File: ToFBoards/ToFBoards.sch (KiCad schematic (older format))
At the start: 1 part, among them U1 VL53L1X

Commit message: ToF boards
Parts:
- added C1: 100n, Capacitors_SMD:C_0402, symbol C_Small
- added C2: 4.7u, Capacitors_SMD:C_0402, symbol C_Small
- added J1: Bottom, footprint:ToFTop, symbol Conn_01x02
- added J2: Top, footprint:ToFBottom, symbol Conn_01x03
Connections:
- net VCC: now reaches U1.1 (AVDDS)
- net VCC: now also U1.11 (AVDD), C1.1, C2.1, J2.1 (Pin_1)
- net SCL: now reaches U1.10 (SCL)
- net SCL: now also J1.1 (Pin_1)
- net GND: now reaches U1.12 (GND4)
- net GND: now also U1.2 (AVSSS), U1.3 (GND1), U1.4 (GND2), U1.6 (GND3), C1.2, C2.2, J2.3 (Pin_3)
- net SIGNAL: now reaches U1.5 (XSHUT)
- net SIGNAL: now also J1.2 (Pin_2)
- net SDA: now reaches U1.9 (SDA)
- net SDA: now also J2.2 (Pin_2)
- no-connect marks 0 -> 2
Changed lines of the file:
@@
 LIBS:valves
 LIBS:parts
+LIBS:ToFBoards-cache
 EELAYER 25 0
 EELAYER END
@@
 	1    0    0    -1
 $EndComp
+Text GLabel 6185 3545 2    39   Input ~ 0
+SCL
+Text GLabel 6185 3755 2    39   Input ~ 0
+SDA
+$Comp
+L C_Small C2
+U 1 1 5B60667F
+P 4530 3220
+F 0 "C2" H 4540 3290 39  0000 L CNN
+F 1 "4.7u" H 4540 3140 39  0000 L CNN
+F 2 "Capacitors_SMD:C_0402" H 4530 3220 50  0001 C CNN
+F 3 "" H 4530 3220 50  0001 C CNN
+	1    4530 3220
+	1    0    0    -1
+$EndComp
+$Comp
+L C_Small C1
+U 1 1 5B606704
+P 4100 3220
+F 0 "C1" H 4110 3290 39  0000 L CNN
+F 1 "100n" H 4110 3140 39  0000 L CNN
+F 2 "Capacitors_SMD:C_0402" H 4100 3220 50  0001 C CNN
+F 3 "" H 4100 3220 50  0001 C CNN
+	1    4100 3220
+	1    0    0    -1
+$EndComp
+Text GLabel 3895 3100 0    39   Input ~ 0
+VCC
+Text GLabel 3895 3650 0    39   Input ~ 0
+GND
+Text GLabel 5145 3860 0    39   Input ~ 0
+SIGNAL
+NoConn ~ 6185 3855
+NoConn ~ 6185 3960
+Wire Wire Line
+	5145 3960 4835 3960
+Wire Wire Line
+	4835 3545 4835 4250
+Wire Wire Line
+	4835 3755 5145 3755
+Wire Wire Line
+	6185 3435 6420 3435
+Wire Wire Line
+	6420 3435 6420 4250
+Wire Wire Line
+	6420 4250 4835 4250
+Connection ~ 4835 3960
+Wire Wire Line
+	3895 3100 6565 3100
+Wire Wire Line
+	4100 3100 4100 3120
+Wire Wire Line
+	4530 3100 4530 3120
+Connection ~ 4100 3100
+Wire Wire Line
+	6565 3100 6565 3650
+Wire Wire Line
+	6565 3650 6185 3650
+Connection ~ 4530 3100
+Wire Wire Line
+	5145 3435 4940 3435
+Wire Wire Line
+	4940 3435 4940 3100
+Connection ~ 4940 3100
+Wire Wire Line
+	4100 3320 4100 3650
+Wire Wire Line
+	3895 3650 5145 3650
+Connection ~ 4100 3650
+Connection ~ 4835 3650
+Connection ~ 4835 3755
+Wire Wire Line
+	4530 3545 5145 3545
+Wire Wire Line
+	4530 3320 4530 3545
+Connection ~ 4835 3545
+$Comp
+L Conn_01x02 J1
+U 1 1 5B606E26
+P 8025 3300
+F 0 "J1" H 8025 3400 50  0000 C CNN
+F 1 "Bottom" H 8025 3100 50  0000 C CNN
+F 2 "footprint:ToFTop" H 8025 3300 50  0001 C CNN
+F 3 "" H 8025 3300 50  0001 C CNN
+	1    8025 3300
+	1    0    0    -1
+$EndComp
+$Comp
+L Conn_01x03 J2
+U 1 1 5B606EF1
+P 8025 3890
+F 0 "J2" H 8025 4090 50  0000 C CNN
+F 1 "Top" H 8025 3690 50  0000 C CNN
+F 2 "footprint:ToFBottom" H 8025 3890 50  0001 C CNN
+F 3 "" H 8025 3890 50  0001 C CNN
+	1    8025 3890
+	1    0    0    -1
+$EndComp
+Text GLabel 7825 3890 0    39   Input ~ 0
+SDA
+Text GLabel 7825 3790 0    39   Input ~ 0
+VCC
+Text GLabel 7825 3990 0    39   Input ~ 0
+GND
+Text GLabel 7825 3400 0    39   Input ~ 0
+SIGNAL
+Text GLabel 7825 3300 0    39   Input ~ 0
+SCL
 $EndSCHEMATC

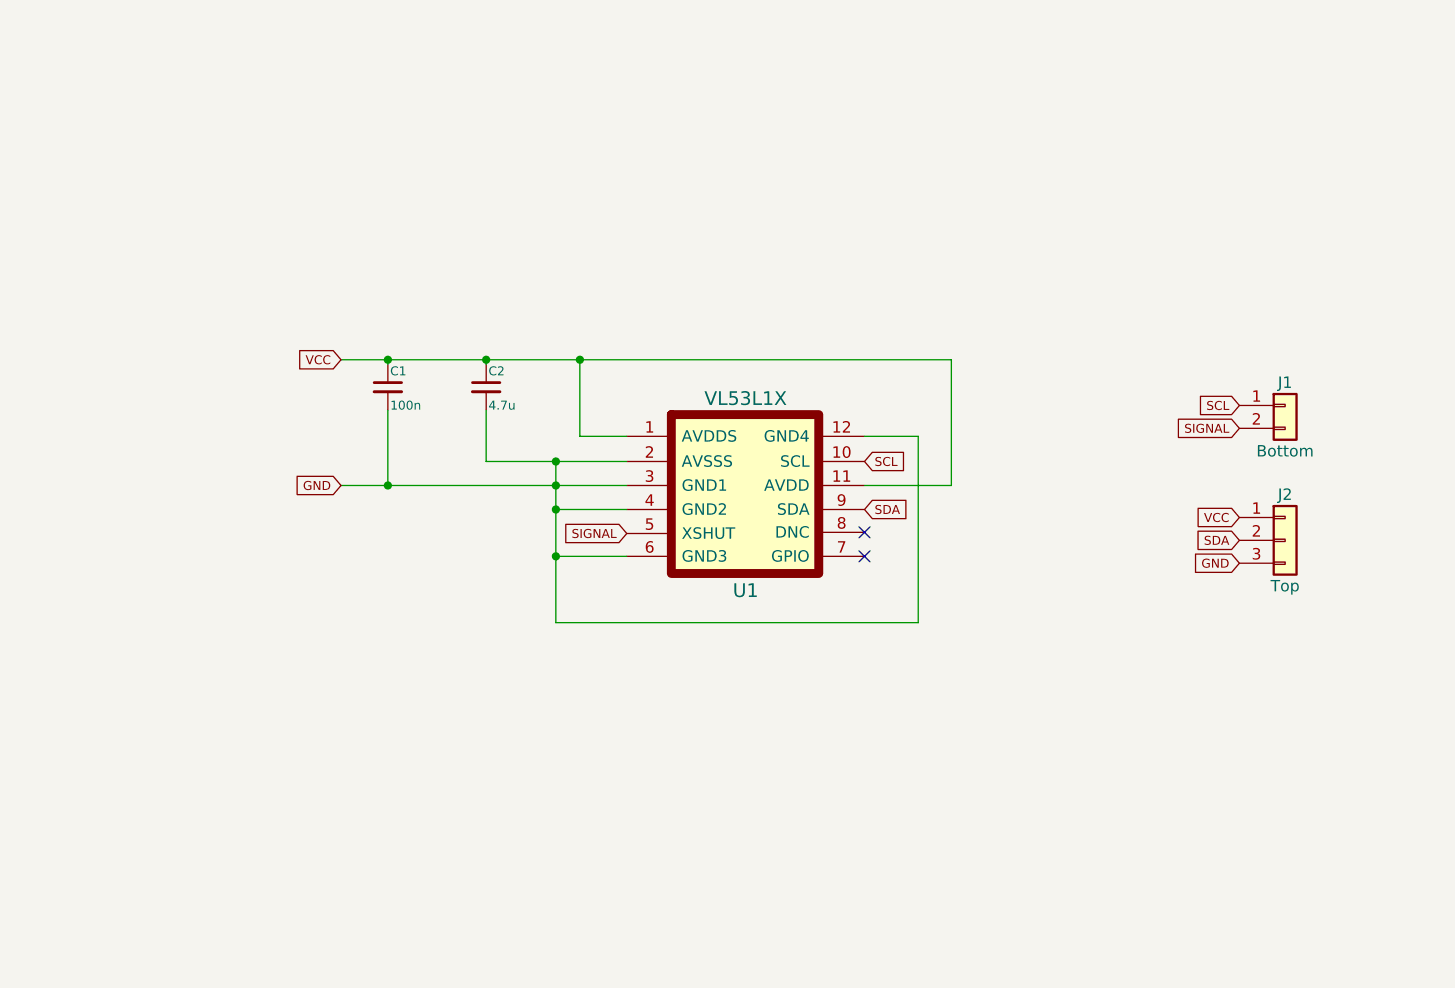
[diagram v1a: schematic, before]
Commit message: complete ToF boards
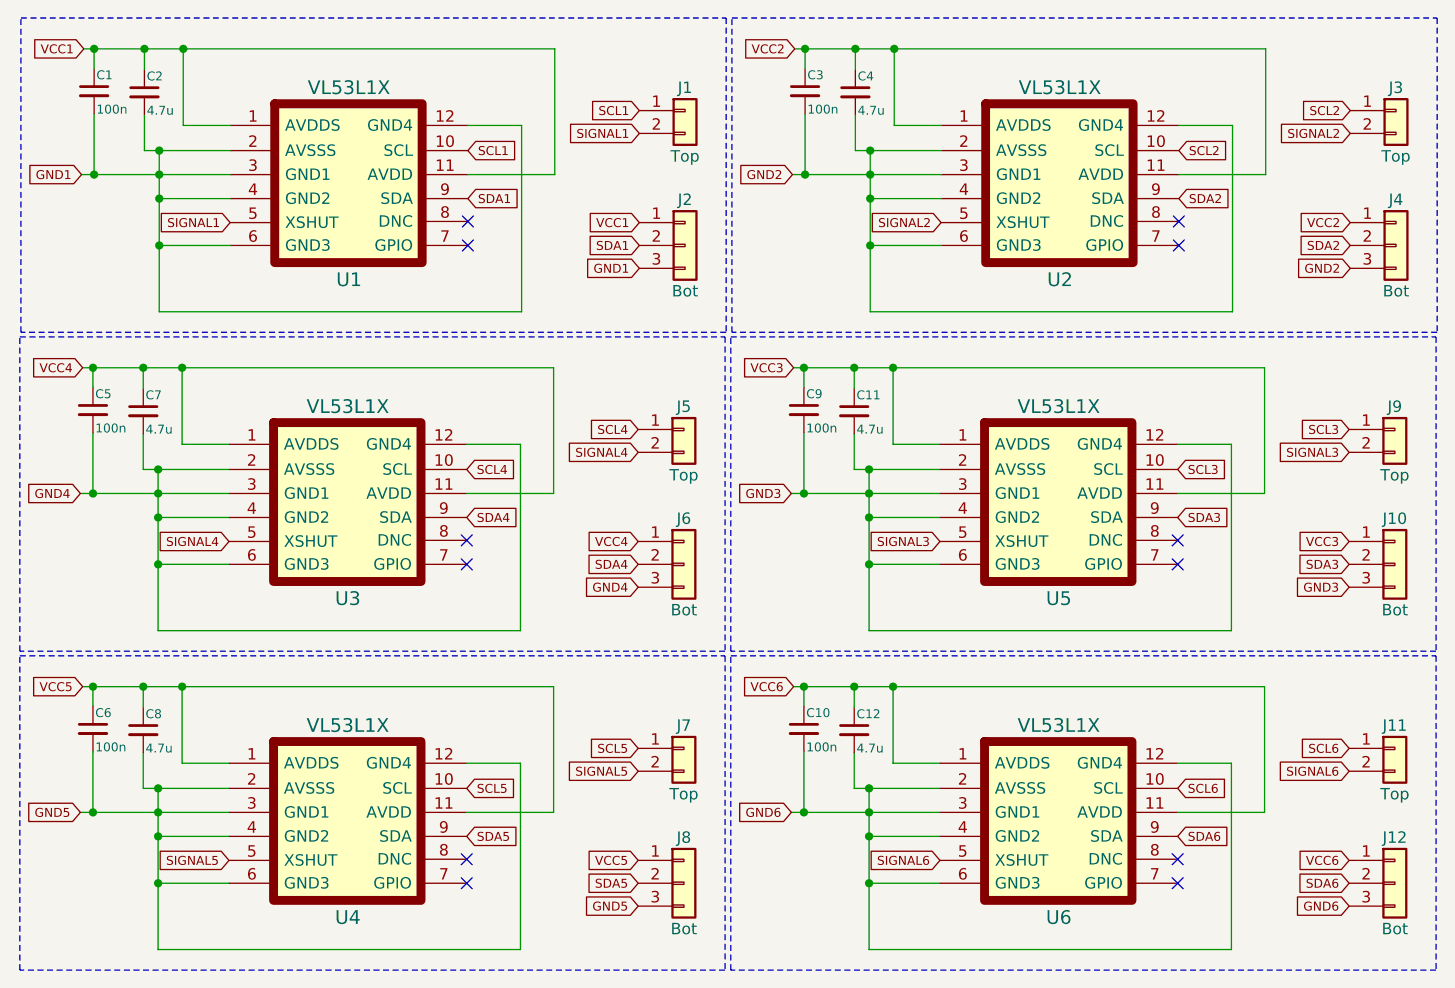
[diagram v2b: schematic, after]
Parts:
- added C10, C3, C5, C6, C9: 100n, Capacitors_SMD:C_0402, symbol C_Small
- added C11, C12, C4, C7, C8: 4.7u, Capacitors_SMD:C_0402, symbol C_Small
- added J10, J12, J4, J6, J8: Bot, footprint:ToFBottom, symbol Conn_01x03
- added J11, J3, J5, J7, J9: Top, footprint:ToFTop, symbol Conn_01x02
- added U2, U3, U4, U5, U6: VL53L1X, footprint:VL53L1X, symbol VL53L1X
- J1: value Bottom -> Top
- J2: value Top -> Bot
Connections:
- net GND renamed GND1
- net SCL renamed SCL1
- net SDA renamed SDA1
- net SIGNAL renamed SIGNAL1
- net VCC renamed VCC1
- new net GND2: C3.2, C4.2, J4.3 (Pin_3), U2.12 (GND4), U2.2 (AVSSS), U2.3 (GND1), U2.4 (GND2), U2.6 (GND3)
- new net GND3: C11.2, C9.2, J10.3 (Pin_3), U5.12 (GND4), U5.2 (AVSSS), U5.3 (GND1), U5.4 (GND2), U5.6 (GND3)
- new net GND4: C5.2, C7.2, J6.3 (Pin_3), U3.12 (GND4), U3.2 (AVSSS), U3.3 (GND1), U3.4 (GND2), U3.6 (GND3)
- new net GND5: C6.2, C8.2, J8.3 (Pin_3), U4.12 (GND4), U4.2 (AVSSS), U4.3 (GND1), U4.4 (GND2), U4.6 (GND3)
- new net GND6: C10.2, C12.2, J12.3 (Pin_3), U6.12 (GND4), U6.2 (AVSSS), U6.3 (GND1), U6.4 (GND2), U6.6 (GND3)
- new net SCL2: J3.1 (Pin_1), U2.10 (SCL)
- new net SCL3: J9.1 (Pin_1), U5.10 (SCL)
- new net SCL4: J5.1 (Pin_1), U3.10 (SCL)
- new net SCL5: J7.1 (Pin_1), U4.10 (SCL)
- new net SCL6: J11.1 (Pin_1), U6.10 (SCL)
- new net SDA2: J4.2 (Pin_2), U2.9 (SDA)
- new net SDA3: J10.2 (Pin_2), U5.9 (SDA)
- new net SDA4: J6.2 (Pin_2), U3.9 (SDA)
- new net SDA5: J8.2 (Pin_2), U4.9 (SDA)
- new net SDA6: J12.2 (Pin_2), U6.9 (SDA)
- new net SIGNAL2: J3.2 (Pin_2), U2.5 (XSHUT)
- new net SIGNAL3: J9.2 (Pin_2), U5.5 (XSHUT)
- new net SIGNAL4: J5.2 (Pin_2), U3.5 (XSHUT)
- new net SIGNAL5: J7.2 (Pin_2), U4.5 (XSHUT)
- new net SIGNAL6: J11.2 (Pin_2), U6.5 (XSHUT)
- new net VCC2: C3.1, C4.1, J4.1 (Pin_1), U2.1 (AVDDS), U2.11 (AVDD)
- new net VCC3: C11.1, C9.1, J10.1 (Pin_1), U5.1 (AVDDS), U5.11 (AVDD)
- new net VCC4: C5.1, C7.1, J6.1 (Pin_1), U3.1 (AVDDS), U3.11 (AVDD)
- new net VCC5: C6.1, C8.1, J8.1 (Pin_1), U4.1 (AVDDS), U4.11 (AVDD)
- new net VCC6: C10.1, C12.1, J12.1 (Pin_1), U6.1 (AVDDS), U6.11 (AVDD)
- no-connect marks 2 -> 12
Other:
- moved on the sheet: C1, C2, J1, J2, U1
